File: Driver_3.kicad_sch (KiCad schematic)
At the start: 26 parts

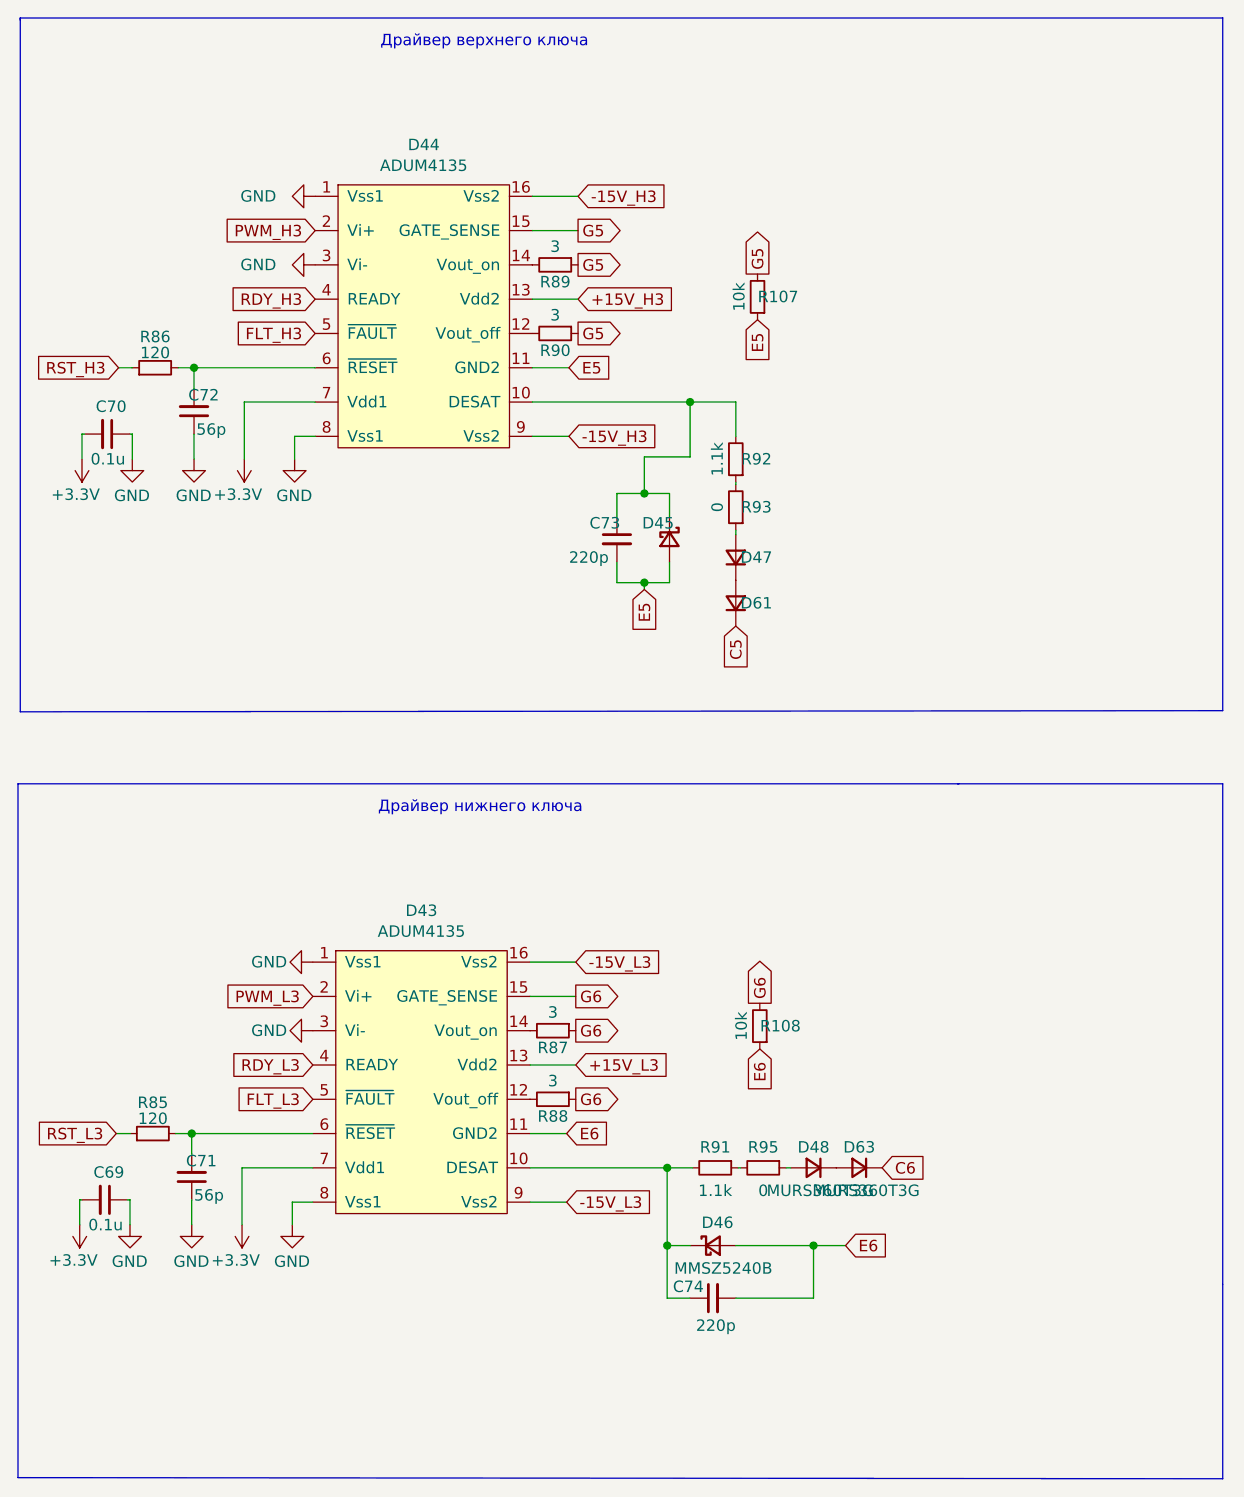
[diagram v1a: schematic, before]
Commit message: Поменял драйвера на китайские
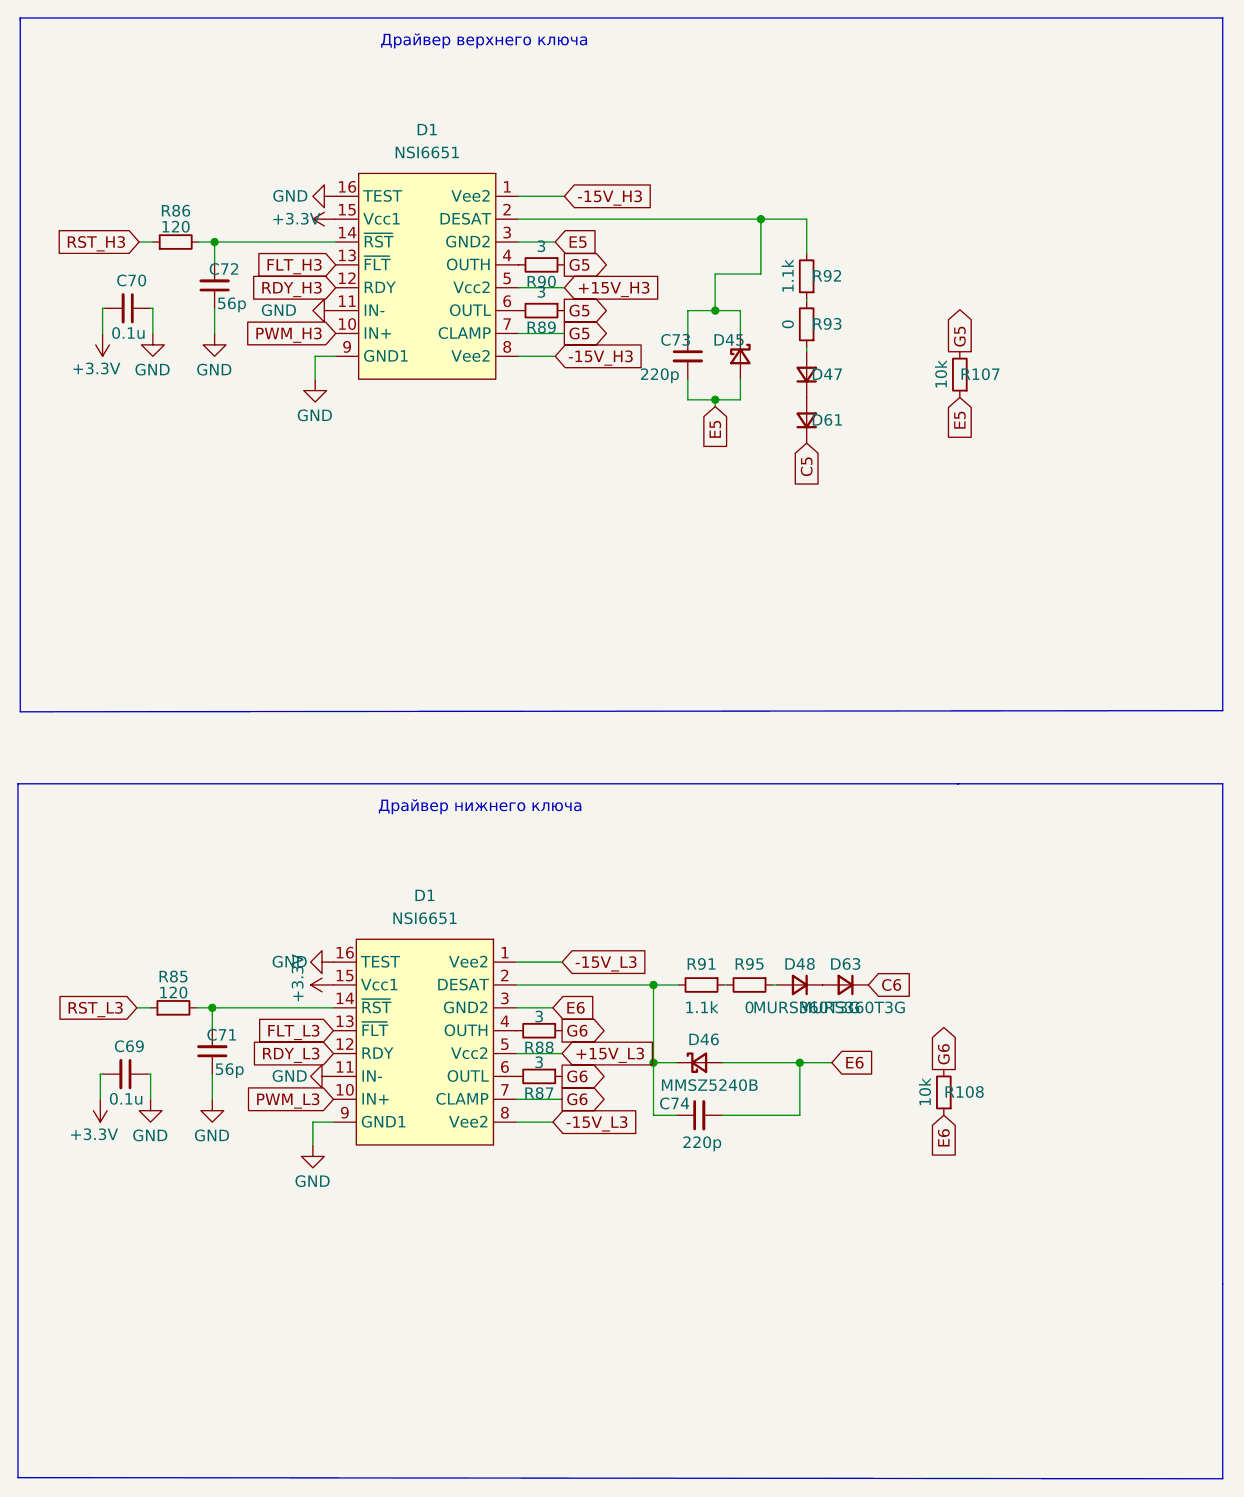
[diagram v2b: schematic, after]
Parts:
- removed D43, D44: ADUM4135, Package_SO:SOIC-16W_7.5x10.3mm_P1.27mm, symbol ADUM_Driver:ADUM4135
- added D1 (x2): NSI6651, Package_SO:SOIC-16W_7.5x10.3mm_P1.27mm, symbol Driver_My:NSI6651
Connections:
- net +15V_H3: now also D1.5 (Vcc2)
- net +15V_L3: now also D1.5 (Vcc2)
- net +3V3: now also D1.15 (Vcc1), D1.15 (Vcc1)
- net -15V_H3: now also D1.1 (Vee2), D1.8 (Vee2)
- net -15V_L3: now also D1.1 (Vee2), D1.8 (Vee2)
- net E5: now also D1.3 (GND2)
- net E6: now also D1.3 (GND2)
- net FLT_H3: now also D1.13 (~{FLT})
- net FLT_L3: now also D1.13 (~{FLT})
- net G5: now also D1.7 (CLAMP)
- net G6: now also D1.7 (CLAMP)
- net GND: now also D1.11 (IN-), D1.11 (IN-), D1.16 (TEST), D1.16 (TEST), D1.9 (GND1), D1.9 (GND1)
- net PWM_H3: now also D1.10 (IN+)
- net PWM_L3: now also D1.10 (IN+)
- net RDY_H3: now also D1.12 (RDY)
- net RDY_L3: now also D1.12 (RDY)
- net at C72.2, R86.2: now also D1.14 (~{RST})
- net at C71.2, R85.2: now also D1.14 (~{RST})
- net at C73.1, D45.1 (K), R92.2: now also D1.2 (DESAT)
- net at R90.2: now also D1.4 (OUTH)
- net at R89.2: now also D1.6 (OUTL)
- net at R88.2: now also D1.4 (OUTH)
- net at C74.1, D46.1 (K), R91.2: now also D1.2 (DESAT)
- net at R87.2: now also D1.6 (OUTL)
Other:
- moved on the sheet: C69, C70, C71, C72, C73, C74, D45, D46, D47, D48, D61, D63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

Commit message: Изменил схему
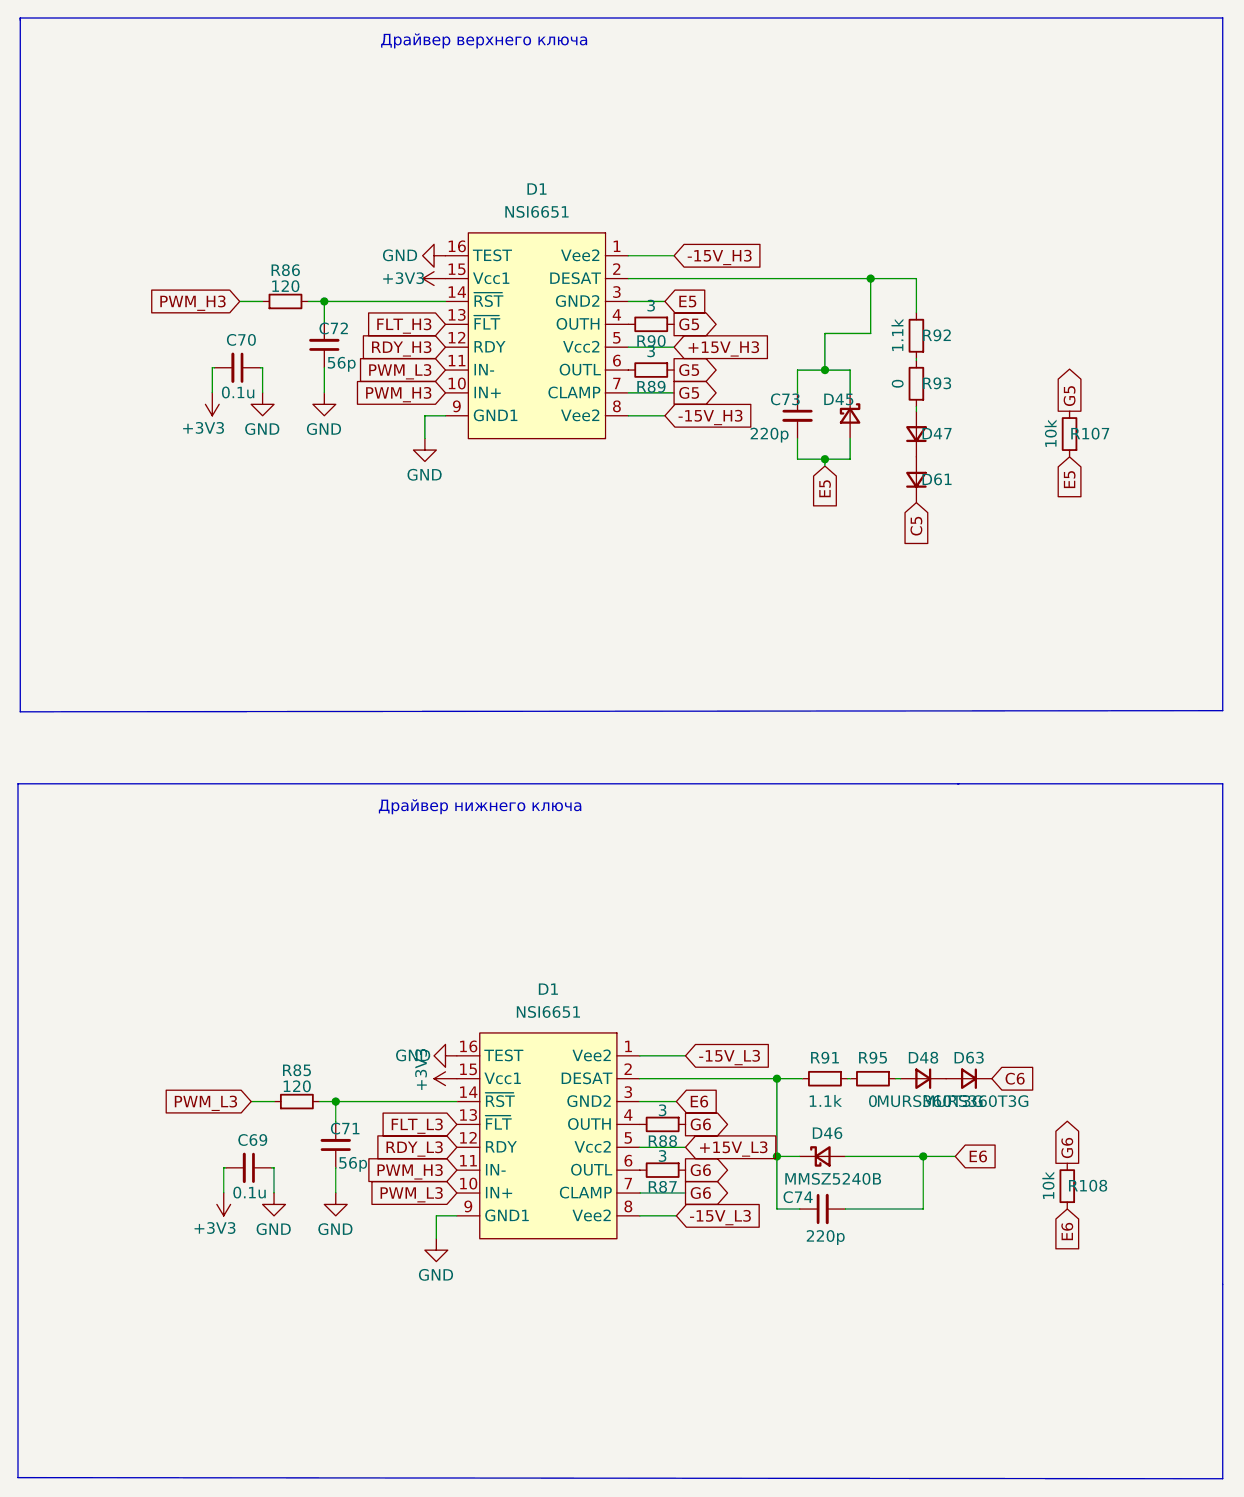
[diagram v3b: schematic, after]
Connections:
- net RST_H3 is gone; now on net PWM_H3: R86.1
- net RST_L3 is gone; now on net PWM_L3: R85.1
- net GND: no longer D1.11 (IN-), D1.11 (IN-)
- net PWM_H3: now also D1.11 (IN-)
- net PWM_L3: now also D1.11 (IN-)
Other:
- moved on the sheet: C69, C70, C71, C72, C73, C74, D1, D45, D46, D47, D48, D61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

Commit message: Разместил все три стойки в своей области
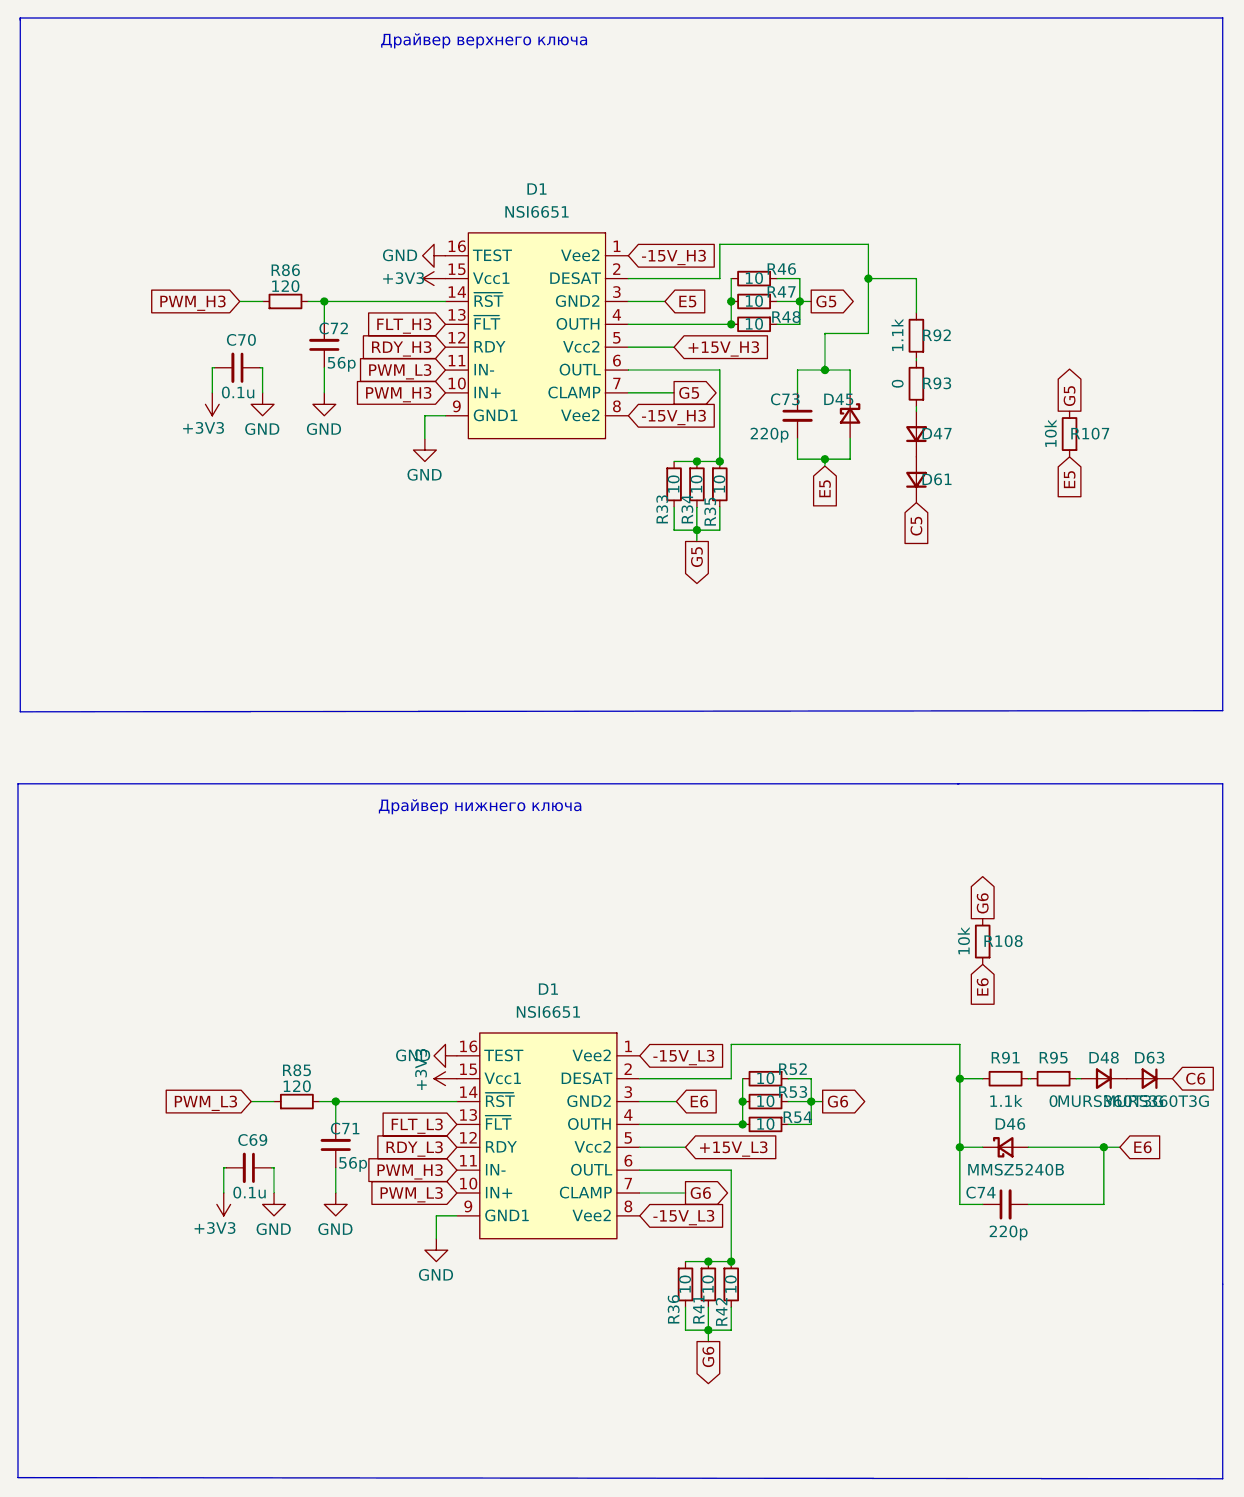
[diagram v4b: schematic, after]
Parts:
- removed R87, R88, R89, R90: 3, Resistor_SMD:R_2512_6332Metric_Pad1.40x3.35mm_HandSolder, symbol Device:R_Small
- added R33, R34, R35, R36, R41, R42, R46, R47, R48, R52, R53, R54: 10, Resistor_SMD:R_1206_3216Metric_Pad1.30x1.75mm_HandSolder, symbol Device:R_Small
- D47, D48, D61, D63: footprint Diode_SMD:D_SMC -> Diode_SMD:D_SMA_Handsoldering
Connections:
- net G5: now also R33.2, R34.2, R35.2, R46.1, R47.1, R48.1
- net G6: now also R36.2, R41.2, R42.2, R52.1, R53.1, R54.1
- net at D1.4 (OUTH): now also R52.2, R53.2, R54.2
- net at D1.4 (OUTH): now also R46.2, R47.2, R48.2
- net at D1.6 (OUTL): now also R33.1, R34.1, R35.1
- net at D1.6 (OUTL): now also R36.1, R41.1, R42.1
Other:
- moved on the sheet: C74, D46, D48, D63, R108, R91, R95

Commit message: Убрал питание 3.3В
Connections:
- net +3V3 renamed +5V
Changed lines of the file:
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@@
 	)
 	(symbol
-		(lib_id "power:+3.3V")
+		(lib_id "power:+5V")
 		(at 80.01 140.97 90)
 		(unit 1)
@@
 		(on_board yes)
 		(dnp no)
-		(property "Reference" "#PWR0196"
+		(property "Reference" "#PWR196"
 			(at 83.82 140.97 0)
 			(effects
@@
 			)
 		)
-		(property "Value" "+3V3"
-			(at 76.073 137.541 0)
-			(effects
-				(font
-					(size 1.27 1.27)
-				)
-				(justify right)
+		(property "Value" "+5V"
+			(at 76.454 140.97 0)
+			(effects
+				(font
+					(size 1.27 1.27)
+				)
 			)
 		)
@@
 			)
 		)
-		(property "Description" ""
+		(property "Description" "Power symbol creates a global label with name \"+5V\""
 			(at 80.01 140.97 0)
 			(effects
@@
 			(project "Adapter"
 				(path "/e63e39d7-6ac0-4ffd-8aa3-1841a4541b55/4f6bfb91-7e0a-4b8d-9918-082ff107cb6c"
-					(reference "#PWR0196")
+					(reference "#PWR196")
 					(unit 1)
 				)
@@
 	)
 	(symbol
-		(lib_id "power:+3.3V")
+		(lib_id "power:+5V")
 		(at 78.74 52.07 90)
 		(unit 1)
@@
 		(on_board yes)
 		(dnp no)
-		(property "Reference" "#PWR0190"
+		(property "Reference" "#PWR190"
 			(at 82.55 52.07 0)
 			(effects
@@
 			)
 		)
-		(property "Value" "+3V3"
-			(at 71.628 52.07 90)
-			(effects
-				(font
-					(size 1.27 1.27)
-				)
-				(justify right)
+		(property "Value" "+5V"
+			(at 75.184 52.07 0)
+			(effects
+				(font
+					(size 1.27 1.27)
+				)
 			)
 		)
@@
 			)
 		)
-		(property "Description" ""
+		(property "Description" "Power symbol creates a global label with name \"+5V\""
 			(at 78.74 52.07 0)
 			(effects
@@
 			(project "Adapter"
 				(path "/e63e39d7-6ac0-4ffd-8aa3-1841a4541b55/4f6bfb91-7e0a-4b8d-9918-082ff107cb6c"
-					(reference "#PWR0190")
+					(reference "#PWR190")
 					(unit 1)
 				)
@@
 	)
 	(symbol
-		(lib_id "power:+3.3V")
+		(lib_id "power:+5V")
 		(at 52.832 64.77 180)
 		(unit 1)
@@
 		(on_board yes)
 		(dnp no)
-		(property "Reference" "#PWR0189"
+		(property "Reference" "#PWR189"
 			(at 52.832 60.96 0)
 			(effects
@@
 			)
 		)
-		(property "Value" "+3V3"
-			(at 49.403 68.707 0)
-			(effects
-				(font
-					(size 1.27 1.27)
-				)
-				(justify right)
+		(property "Value" "+5V"
+			(at 52.832 68.326 0)
+			(effects
+				(font
+					(size 1.27 1.27)
+				)
 			)
 		)
@@
 			)
 		)
-		(property "Description" ""
+		(property "Description" "Power symbol creates a global label with name \"+5V\""
 			(at 52.832 64.77 0)
 			(effects
@@
 			(project "Adapter"
 				(path "/e63e39d7-6ac0-4ffd-8aa3-1841a4541b55/4f6bfb91-7e0a-4b8d-9918-082ff107cb6c"
-					(reference "#PWR0189")
+					(reference "#PWR189")
 					(unit 1)
 				)
@@
 	)
 	(symbol
-		(lib_id "power:+3.3V")
+		(lib_id "power:+5V")
 		(at 54.102 153.67 180)
 		(unit 1)
@@
 		(on_board yes)
 		(dnp no)
-		(property "Reference" "#PWR0195"
+		(property "Reference" "#PWR195"
 			(at 54.102 149.86 0)
 			(effects
@@
 			)
 		)
-		(property "Value" "+3V3"
-			(at 50.673 157.607 0)
-			(effects
-				(font
-					(size 1.27 1.27)
-				)
-				(justify right)
+		(property "Value" "+5V"
+			(at 54.102 157.226 0)
+			(effects
+				(font
+					(size 1.27 1.27)
+				)
 			)
 		)
@@
 			)
 		)
-		(property "Description" ""
+		(property "Description" "Power symbol creates a global label with name \"+5V\""
 			(at 54.102 153.67 0)
 			(effects
@@
 			(project "Adapter"
 				(path "/e63e39d7-6ac0-4ffd-8aa3-1841a4541b55/4f6bfb91-7e0a-4b8d-9918-082ff107cb6c"
-					(reference "#PWR0195")
-					(unit 1)
-				)
+					(reference "#PWR195")
+					(unit 1)
+				)
